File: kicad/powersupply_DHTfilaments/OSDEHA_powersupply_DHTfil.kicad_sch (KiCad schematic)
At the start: 6 parts, among them J1 10.5 VAC / 4.5 A, J2 10.5 VAC / 4.5 A, J3 COLEMANREG-LEFT-1, J4 COLEMANREG-LEFT-2, J5 COLEMANREG-RIGHT-1, J6 COLEMANREG-RIGHT-2

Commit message: up
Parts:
- added H1, H2, H3, H4: MountingHole, MountingHole:MountingHole_3.2mm_M3, symbol Mechanical:MountingHole

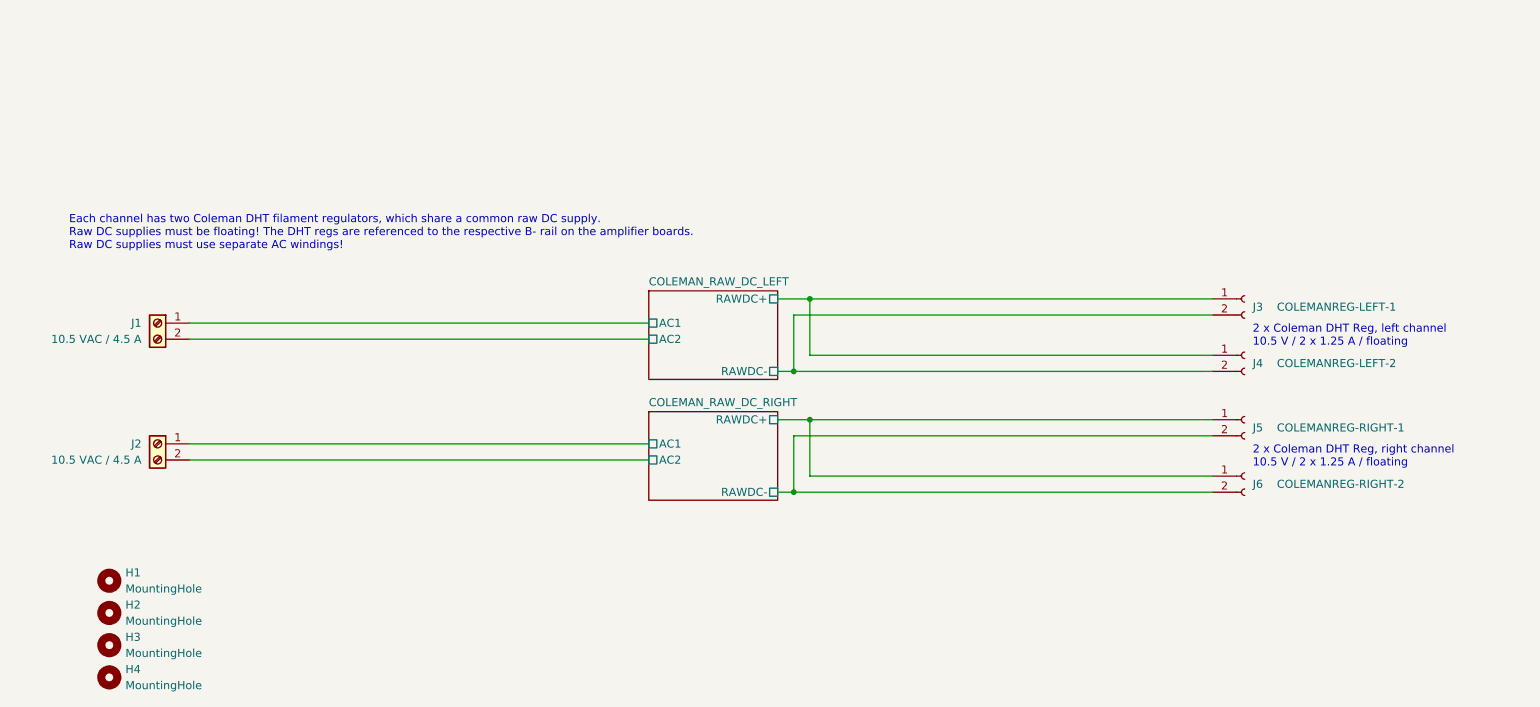
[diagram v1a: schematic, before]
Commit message: improved + simplified wiring/connections to DHT filaments, improved pin/net labels
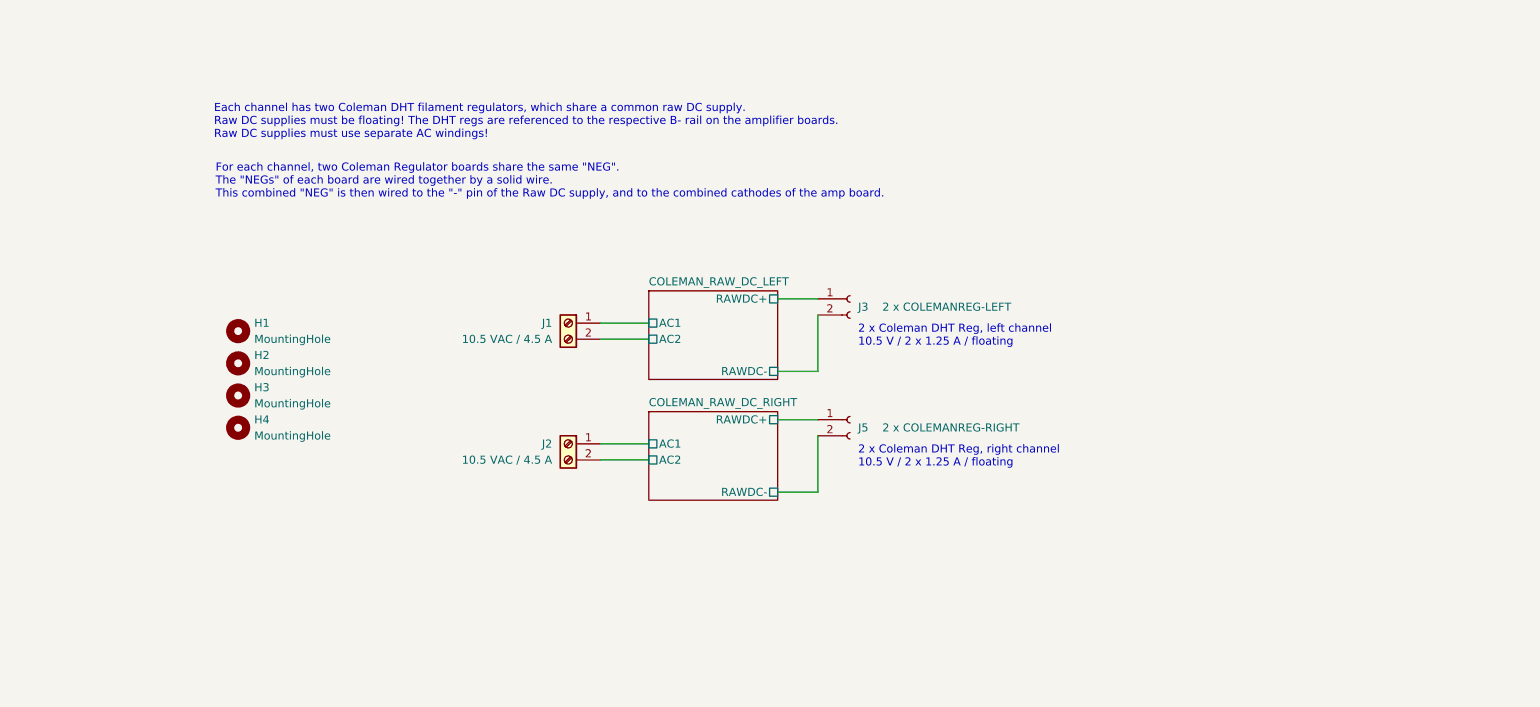
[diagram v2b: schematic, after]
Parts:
- removed J4: COLEMANREG-LEFT-2, Connector_Molex:Molex_KK-396_A-41791-0002_1x02_P3.96mm_Vertical, symbol Connector:Conn_01x02_Socket
- removed J6: COLEMANREG-RIGHT-2, Connector_Molex:Molex_KK-396_A-41791-0002_1x02_P3.96mm_Vertical, symbol Connector:Conn_01x02_Socket
- J3: value COLEMANREG-LEFT-1 -> 2 x COLEMANREG-LEFT
- J5: value COLEMANREG-RIGHT-1 -> 2 x COLEMANREG-RIGHT
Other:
- note added: "For each channel, two Coleman Regulator boards share the same "NEG". The "NEGs" of each board are wired together by a solid wire. This combined "NEG" is then wired to the "-" pin of the Raw DC supply, and to the combined cathodes of the amp board."
- moved on the sheet: H1, H2, H3, H4, J1, J2, J3, J5

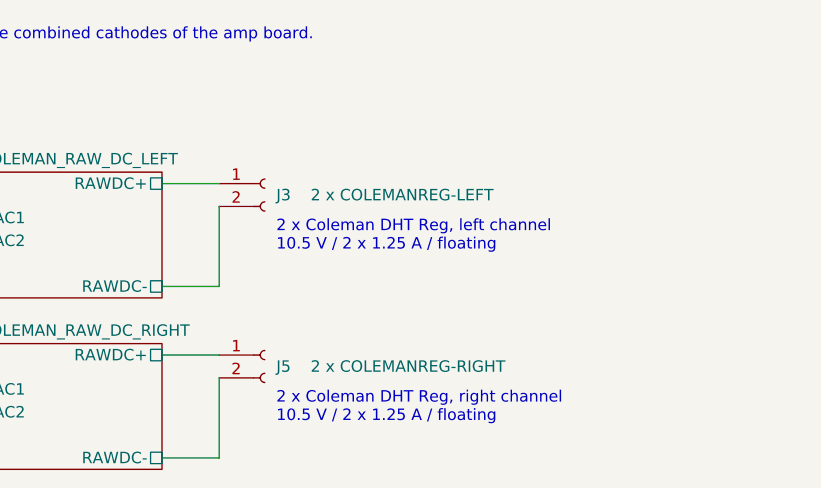
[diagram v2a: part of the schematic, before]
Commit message: added pin labels
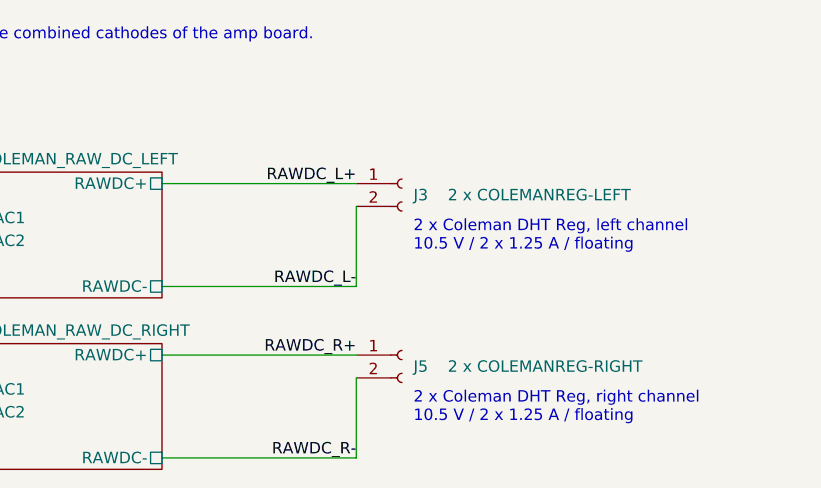
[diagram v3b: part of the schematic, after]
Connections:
- net COLEMAN_RAW_DC_LEFT/RAWDC+ renamed RAWDC_L+
- net COLEMAN_RAW_DC_LEFT/RAWDC- renamed RAWDC_L-
- net COLEMAN_RAW_DC_RIGHT/RAWDC+ renamed RAWDC_R+
- net COLEMAN_RAW_DC_RIGHT/RAWDC- renamed RAWDC_R-
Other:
- moved on the sheet: J3, J5
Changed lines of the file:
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@@
 	(wire
 		(pts
-			(xy 149.86 60.96) (xy 156.21 60.96)
-		)
-		(stroke
-			(width 0)
-			(type default)
-		)
-	)
-	(wire
-		(pts
-			(xy 149.86 72.39) (xy 156.21 72.39)
+			(xy 149.86 60.96) (xy 171.45 60.96)
+		)
+		(stroke
+			(width 0)
+			(type default)
+		)
+	)
+	(wire
+		(pts
+			(xy 149.86 72.39) (xy 171.45 72.39)
 		)
 		(stroke
@@
 	(wire
 		(pts
-			(xy 156.21 63.5) (xy 156.21 72.39)
-		)
-		(stroke
-			(width 0)
-			(type default)
-		)
-	)
-	(wire
-		(pts
-			(xy 149.86 80.01) (xy 156.21 80.01)
-		)
-		(stroke
-			(width 0)
-			(type default)
-		)
-	)
-	(wire
-		(pts
-			(xy 149.86 91.44) (xy 156.21 91.44)
+			(xy 149.86 80.01) (xy 171.45 80.01)
+		)
+		(stroke
+			(width 0)
+			(type default)
+		)
+	)
+	(wire
+		(pts
+			(xy 171.45 72.39) (xy 171.45 63.5)
+		)
+		(stroke
+			(width 0)
+			(type default)
+		)
+	)
+	(wire
+		(pts
+			(xy 149.86 91.44) (xy 171.45 91.44)
+		)
+		(stroke
+			(width 0)
+			(type default)
+		)
+	)
+	(wire
+		(pts
+			(xy 171.45 91.44) (xy 171.45 82.55)
 		)
 		(stroke
@@
 		)
 	)
-	(wire
-		(pts
-			(xy 156.21 82.55) (xy 156.21 91.44)
-		)
-		(stroke
-			(width 0)
-			(type default)
-		)
-	)
 	(text "2 x Coleman DHT Reg, left channel\n10.5 V / 2 x 1.25 A / floating"
 		(exclude_from_sim no)
-		(at 162.56 68.58 0)
+		(at 177.8 68.58 0)
 		(effects
 			(font
@@
 	(text "2 x Coleman DHT Reg, right channel\n10.5 V / 2 x 1.25 A / floating"
 		(exclude_from_sim no)
-		(at 162.56 87.63 0)
+		(at 177.8 87.63 0)
 		(effects
 			(font
@@
 			)
 			(justify left bottom)
+		)
+	)
+	(label "RAWDC_R-"
+		(at 171.45 91.44 180)
+		(effects
+			(font
+				(size 1.27 1.27)
+			)
+			(justify right bottom)
+		)
+	)
+	(label "RAWDC_R+"
+		(at 171.45 80.01 180)
+		(effects
+			(font
+				(size 1.27 1.27)
+			)
+			(justify right bottom)
+		)
+	)
+	(label "RAWDC_L-"
+		(at 171.45 72.39 180)
+		(effects
+			(font
+				(size 1.27 1.27)
+			)
+			(justify right bottom)
+		)
+	)
+	(label "RAWDC_L+"
+		(at 171.45 60.96 180)
+		(effects
+			(font
+				(size 1.27 1.27)
+			)
+			(justify right bottom)
 		)
 	)
@@
 	(symbol
 		(lib_id "Connector:Conn_01x02_Socket")
-		(at 161.29 80.01 0)
+		(at 176.53 80.01 0)
 		(unit 1)
 		(exclude_from_sim no)
@@
 		(dnp no)
 		(property "Reference" "J5"
-			(at 162.56 81.28 0)
+			(at 177.8 81.28 0)
 			(effects
 				(font
@@
 		)
 		(property "Value" "2 x COLEMANREG-RIGHT"
-			(at 166.37 81.28 0)
+			(at 181.61 81.28 0)
 			(effects
 				(font
@@
 		)
 		(property "Footprint" "Connector_Molex:Molex_KK-396_A-41791-0002_1x02_P3.96mm_Vertical"
-			(at 161.29 80.01 0)
+			(at 176.53 80.01 0)
 			(effects
 				(font
@@
 		)
 		(property "Datasheet" "https://www.molex.com/en-us/products/part-detail/417910849?display=pdf"
-			(at 161.29 80.01 0)
+			(at 176.53 80.01 0)
 			(effects
 				(font
@@
 		)
 		(property "Description" ""
-			(at 161.29 80.01 0)
+			(at 176.53 80.01 0)
 			(effects
 				(font
@@
 		)
 		(property "MPN" "41791-0849"
-			(at 161.29 80.01 0)
+			(at 176.53 80.01 0)
 			(effects
 				(font
@@
 	(symbol
 		(lib_id "Connector:Conn_01x02_Socket")
-		(at 161.29 60.96 0)
+		(at 176.53 60.96 0)
 		(unit 1)
 		(exclude_from_sim no)
@@
 		(dnp no)
 		(property "Reference" "J3"
-			(at 162.56 62.23 0)
+			(at 177.8 62.23 0)
 			(effects
 				(font
@@
 		)
 		(property "Value" "2 x COLEMANREG-LEFT"
-			(at 166.37 62.23 0)
+			(at 181.61 62.23 0)
 			(effects
 				(font
@@
 		)
 		(property "Footprint" "Connector_Molex:Molex_KK-396_A-41791-0002_1x02_P3.96mm_Vertical"
-			(at 161.29 60.96 0)
+			(at 176.53 60.96 0)
 			(effects
 				(font
@@
 		)
 		(property "Datasheet" "https://www.molex.com/en-us/products/part-detail/417910849?display=pdf"
-			(at 161.29 60.96 0)
+			(at 176.53 60.96 0)
 			(effects
 				(font
@@
 		)
 		(property "Description" ""
-			(at 161.29 60.96 0)
+			(at 176.53 60.96 0)
 			(effects
 				(font
@@
 		)
 		(property "MPN" "41791-0849"
-			(at 161.29 60.96 0)
-			(effects
-				(font
+			(at 176.53 60.96 0)
+			(effects
+				(font

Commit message: work on DC raw supply PCB
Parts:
- removed J1, J2: 10.5 VAC / 4.5 A, TerminalBlock_Phoenix:TerminalBlock_Phoenix_MKDS-1,5-2-5.08_1x02_P5.08mm_Horizontal, symbol Connector:Screw_Terminal_01x02
- removed J3: 2 x COLEMANREG-LEFT, Connector_Molex:Molex_KK-396_A-41791-0002_1x02_P3.96mm_Vertical, symbol Connector:Conn_01x02_Socket
- removed J5: 2 x COLEMANREG-RIGHT, Connector_Molex:Molex_KK-396_A-41791-0002_1x02_P3.96mm_Vertical, symbol Connector:Conn_01x02_Socket
- added AC1: 10.5 VAC / 4.5 A, TerminalBlock_Phoenix:TerminalBlock_Phoenix_MKDS-1,5-2-5.08_1x02_P5.08mm_Horizontal, symbol Connector:Screw_Terminal_01x02
- added C1, C2: 15000u 25 V, Capacitor_THT:CP_Radial_D25.0mm_P10.00mm_SnapIn, symbol Device:C_Polarized
- added D1, D2, D3, D4: 1N5822, Diode_THT:D_DO-201AD_P15.24mm_Horizontal, symbol Diode:1N5822
- added DC1: 2 x COLEMANREGs, Connector_Molex:Molex_KK-396_A-41791-0002_1x02_P3.96mm_Vertical, symbol Connector:Conn_01x02_Socket
- added R1: 10k, Resistor_THT:R_Axial_DIN0207_L6.3mm_D2.5mm_P2.54mm_Vertical, symbol Device:R
- added R2, R3: 0.22 3 W, Resistor_THT:R_Axial_DIN0414_L11.9mm_D4.5mm_P5.08mm_Vertical, symbol Device:R
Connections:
- new net AC1: AC1.1 (Pin_1), D1.2 (A), D3.1 (K)
- new net AC2: AC1.2 (Pin_2), D2.2 (A), D4.1 (K)
- new net DC+: C2.1, DC1.1 (Pin_1), R2.2
- new net DC-: C2.2, DC1.2 (Pin_2), R3.2
- new net R+: C1.1, D1.1 (K), D2.1 (K), R1.1, R2.1
- new net R-: C1.2, D3.2 (A), D4.2 (A), R1.2, R3.1
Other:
- removed sheet COLEMAN_RAW_DC_LEFT
- removed sheet COLEMAN_RAW_DC_RIGHT
- note added: "Raw DC supply for Coleman DHT filament regulator (floating!)"
- note added: "This PCB provides the raw DC supply for a pair of Coleman DHT Filament Regulators. Two of these PCBs are needed for a stereo amp. Each channel uses one pair of Coleman DHT filament regulators, which share a common raw DC supply. Within a given pair/channel, the "NEG" (INPUT-, OUT-) of each Coleman DHT board are linked together using a solid wire. The "NEG" of each pair/channel connects to B- rail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"
- note removed: "2 x Coleman DHT Reg, left channel 10.5 V / 2 x 1.25 A / floating"
- note removed: "2 x Coleman DHT Reg, right channel 10.5 V / 2 x 1.25 A / floating"
- note removed: "Each channel has two Coleman DHT filament regulators, which share a common raw DC supply. Raw DC supplies must be floating! The DHT regs are referenced to the respective B- rail on the amplifier boards. Raw DC supplies must use separate AC windings!"
- note removed: "For each channel, two Coleman Regulator boards share the same "NEG". The "NEGs" of each board are wired together by a solid wire. This combined "NEG" is then wired to the "-" pin of the Raw DC supply, and to the combined cathodes of the amp board."
- moved on the sheet: H1, H2, H3, H4

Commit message: work on RAW DC supply, various other cleanup things.
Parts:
- C2: MPN SLPX153M025C7P3 -> SLPX153M025C7P3
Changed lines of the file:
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@@
 	(label "DC+"
 		(at 147.32 58.42 180)
+		(fields_autoplaced yes)
 		(effects
 			(font
@@
 	(label "DC-"
 		(at 147.32 60.96 180)
+		(fields_autoplaced yes)
 		(effects
 			(font
@@
 	(label "AC1"
 		(at 62.23 58.42 180)
+		(fields_autoplaced yes)
 		(effects
 			(font
@@
 	(label "AC2"
 		(at 62.23 60.96 180)
+		(fields_autoplaced yes)
 		(effects
 			(font
@@
 			)
 		)
-		(property "MPN" "SLPX153M025C7P3 "
+		(property "MPN" "SLPX153M025C7P3"
 			(at 129.54 59.69 0)
 			(effects

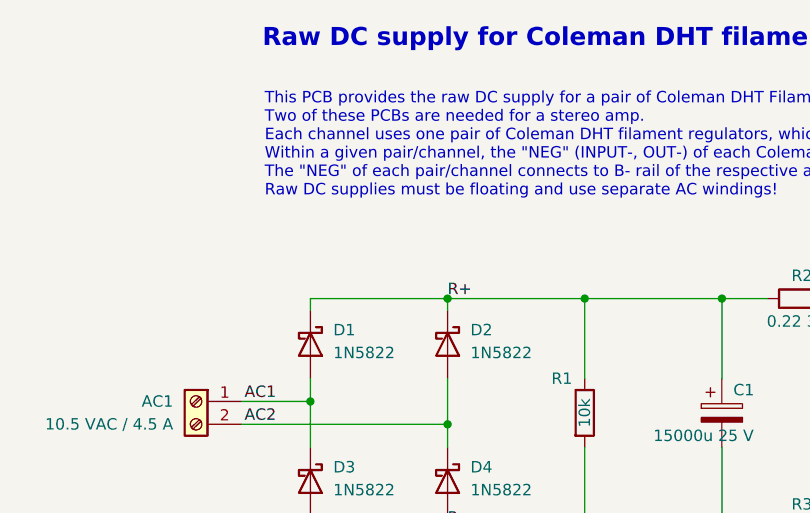
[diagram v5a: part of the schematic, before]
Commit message: add version label to DC raw supply (schematic and PCB)
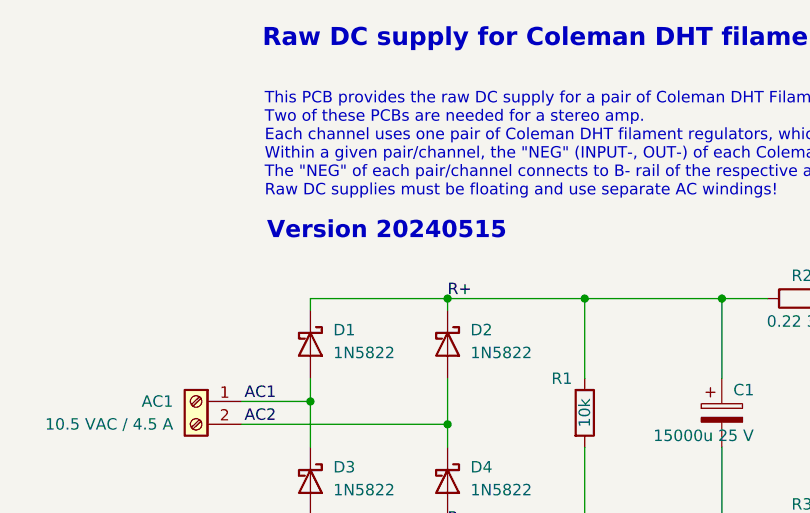
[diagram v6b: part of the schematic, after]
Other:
- note added: "Version 20240515"
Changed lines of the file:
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@@
+		)
+	)
+	(text "Version 20240515"
+		(exclude_from_sim no)
+		(at 61.214 40.64 0)
+		(effects
+			(font
+				(size 1.905 1.905)
+				(thickness 0.381)
+				(bold yes)
+			)
+			(justify left bottom)
 		)
 	)
